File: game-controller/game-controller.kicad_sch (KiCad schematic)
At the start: 0 parts

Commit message: Fixed kicad library manager bug
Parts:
- added U1: STM32F103C8T6, parts:LQFP-48_L7.0-W7.0-P0.50-LS9.0-BL, symbol parts:STM32F103C8T6
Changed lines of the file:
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@@
 	(generator_version "10.0")
 	(paper "A4")
+	(symbol
+		(lib_id "parts:STM32F103C8T6")
+		(at 132.08 93.98 0)
+		(unit 1)
+		(body_style 1)
+		(exclude_from_sim no)
+		(in_bom yes)
+		(on_board yes)
+		(in_pos_files yes)
+		(dnp no)
+		(fields_autoplaced yes)
+		(property "Reference" "U1"
+			(at 132.08 57.15 0)
+			(show_name no)
+			(do_not_autoplace no)
+			(effects
+				(font
+					(size 1.27 1.27)
+				)
+			)
+		)
+		(property "Value" "STM32F103C8T6"
+			(at 132.08 59.69 0)
+			(show_name no)
+			(do_not_autoplace no)
+			(effects
+				(font
+					(size 1.27 1.27)
+				)
+			)
+		)
+		(property "Footprint" "parts:LQFP-48_L7.0-W7.0-P0.50-LS9.0-BL"
+			(at 132.08 130.81 0)
+			(hide yes)
+			(show_name no)
+			(do_not_autoplace no)
+			(effects
+				(font
+					(size 1.27 1.27)
+				)
+			)
+		)
+		(property "Datasheet" "https://lcsc.com/product-detail/ST-Microelectronics_STMicroelectronics_STM32F103C8T6_STM32F103C8T6_C8734.html"
+			(at 132.08 133.35 0)
+			(hide yes)
+			(show_name no)
+			(do_not_autoplace no)
+			(effects
+				(font
+					(size 1.27 1.27)
+				)
+			)
+		)
+		(property "Description" "ARM Cortex-M3 32-bit MCU, 64 KB Flash, 20 KB Internal RAM, 37 IOs, 48-pin LQFP, -40 to 85 degC, Tray"
+			(at 132.08 93.98 0)
+			(hide yes)
+			(show_name no)
+			(do_not_autoplace no)
+			(effects
+				(font
+					(size 1.27 1.27)
+				)
+			)
+		)
+		(property "Manufacturer" "ST(意法半导体)"
+			(at 132.08 135.89 0)
+			(hide yes)
+			(show_name no)
+			(do_not_autoplace no)
+			(effects
+				(font
+					(size 1.27 1.27)
+				)
+			)
+		)
+		(property "MPN" "STM32F103C8T6"
+			(at 132.08 138.43 0)
+			(hide yes)
+			(show_name no)
+			(do_not_autoplace no)
+			(effects
+				(font
+					(size 1.27 1.27)
+				)
+			)
+		)
+		(property "LCSC Part" "C8734"
+			(at 132.08 140.97 0)
+			(hide yes)
+			(show_name no)
+			(do_not_autoplace no)
+			(effects
+				(font
+					(size 1.27 1.27)
+				)
+			)
+		)
+		(pin "15"
+		)
+		(pin "30"
+		)
+		(pin "41"
+		)
+		(pin "28"
+		)
+		(pin "27"
+		)
+		(pin "26"
+		)
+		(pin "17"
+		)
+		(pin "25"
+		)
+		(pin "32"
+		)
+		(pin "24"
+		)
+		(pin "23"
+		)
+		(pin "22"
+		)
+		(pin "21"
+		)
+		(pin "20"
+		)
+		(pin "18"
+		)
+		(pin "19"
+		)
+		(pin "34"
+		)
+		(pin "48"
+		)
+		(pin "47"
+		)
+		(pin "9"
+		)
+		(pin "8"
+		)
+		(pin "7"
+		)
+		(pin "6"
+		)
+		(pin "5"
+		)
+		(pin "4"
+		)
+		(pin "3"
+		)
+		(pin "2"
+		)
+		(pin "1"
+		)
+		(pin "46"
+		)
+		(pin "45"
+		)
+		(pin "29"
+		)
+		(pin "13"
+		)
+		(pin "12"
+		)
+		(pin "11"
+		)
+		(pin "10"
+		)
+		(pin "44"
+		)
+		(pin "33"
+		)
+		(pin "43"
+		)
+		(pin "31"
+		)
+		(pin "42"
+		)
+		(pin "16"
+		)
+		(pin "14"
+		)
+		(pin "40"
+		)
+		(pin "38"
+		)
+		(pin "36"
+		)
+		(pin "37"
+		)
+		(pin "39"
+		)
+		(pin "35"
+		)
+		(instances
+			(project "game-controller"
+				(path "/09f2e687-94b8-4ec9-a79c-a1fb25df92c9"
+					(reference "U1")
+					(unit 1)
+				)
+			)
+		)
+	)
 	(sheet_instances
 		(path "/"

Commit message: Schematics to be continued
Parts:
- added C1, C2, C3: 100nF, symbol Device:C
- added C4: 4.7uF, symbol Device:C
- added C5: 10nF, symbol Device:C
- added C6: 1uF, symbol Device:C
- added FPC1, FPC2: AFC07-S05FCC-00, parts:FPC-SMD_AFC07-S05FCC-00, symbol parts:AFC07-S05FCC-00
- added H1: HX PZ2.54-1X5P WT, parts:HDR-SMD_5P-P2.54-H-M-W12.8-N, symbol parts:HXPZ2.54-1X5PWT
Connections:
- net +3.3V: now reaches U1.1 (VBAT)
- net +3.3V: now also U1.24 (VDD_1), U1.36 (VDD_2), U1.48 (VDD_3), U1.9 (VDDA), C1.1, C2.2, C3.1, C4.1, C5.2, C6.2, H1.5
- net GND: now reaches U1.23 (VSS_1)
- net GND: now also U1.35 (VSS_2), U1.47 (VSS_3), U1.8 (VSSA), C1.2, C2.1, C3.2, C4.2, C5.1, C6.1, FPC1.6, FPC1.7, FPC2.6, FPC2.7, H1.3
- net USB_DM: now reaches U1.32 (PA11)
- net USB_DP: now reaches U1.33 (PA12)
- net SWDIO: now reaches U1.34 (PA13)
- net SWDIO: now also H1.2
- net SWCLK: now reaches U1.37 (PA14)
- net SWCLK: now also H1.4
- net NRST: now reaches U1.7 (NRST)
- net NRST: now also H1.1
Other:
- note added: "https://github.com/dekuNukem/Nintendo_Switch_Reverse_Engineering/issues/69"

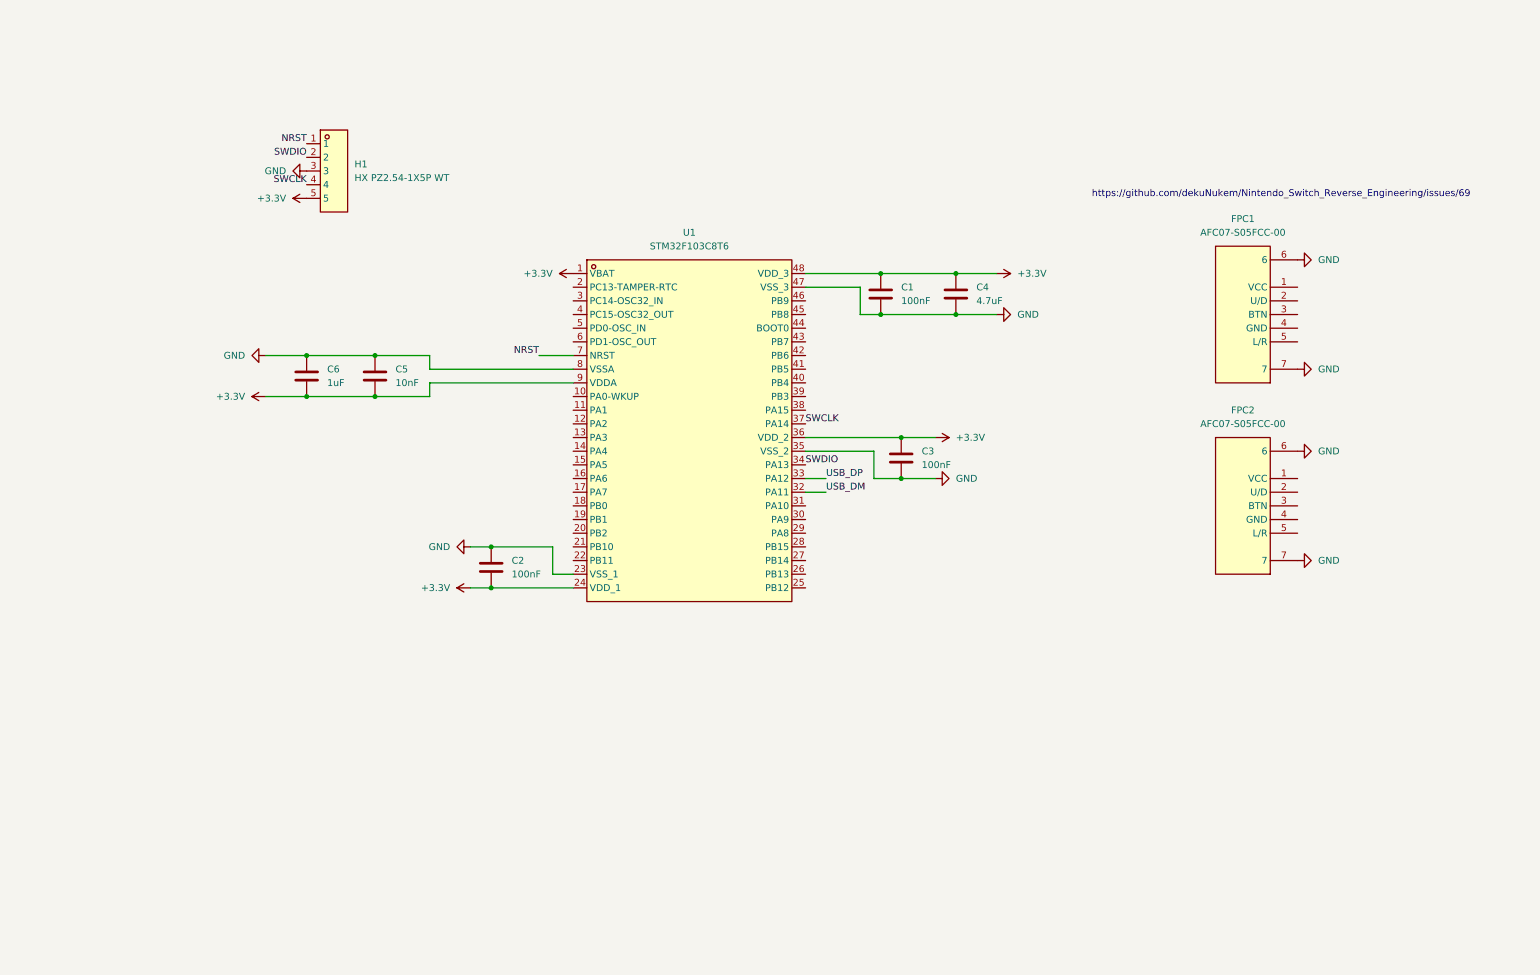
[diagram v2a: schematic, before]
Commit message: Added dpad and buttons to schematics
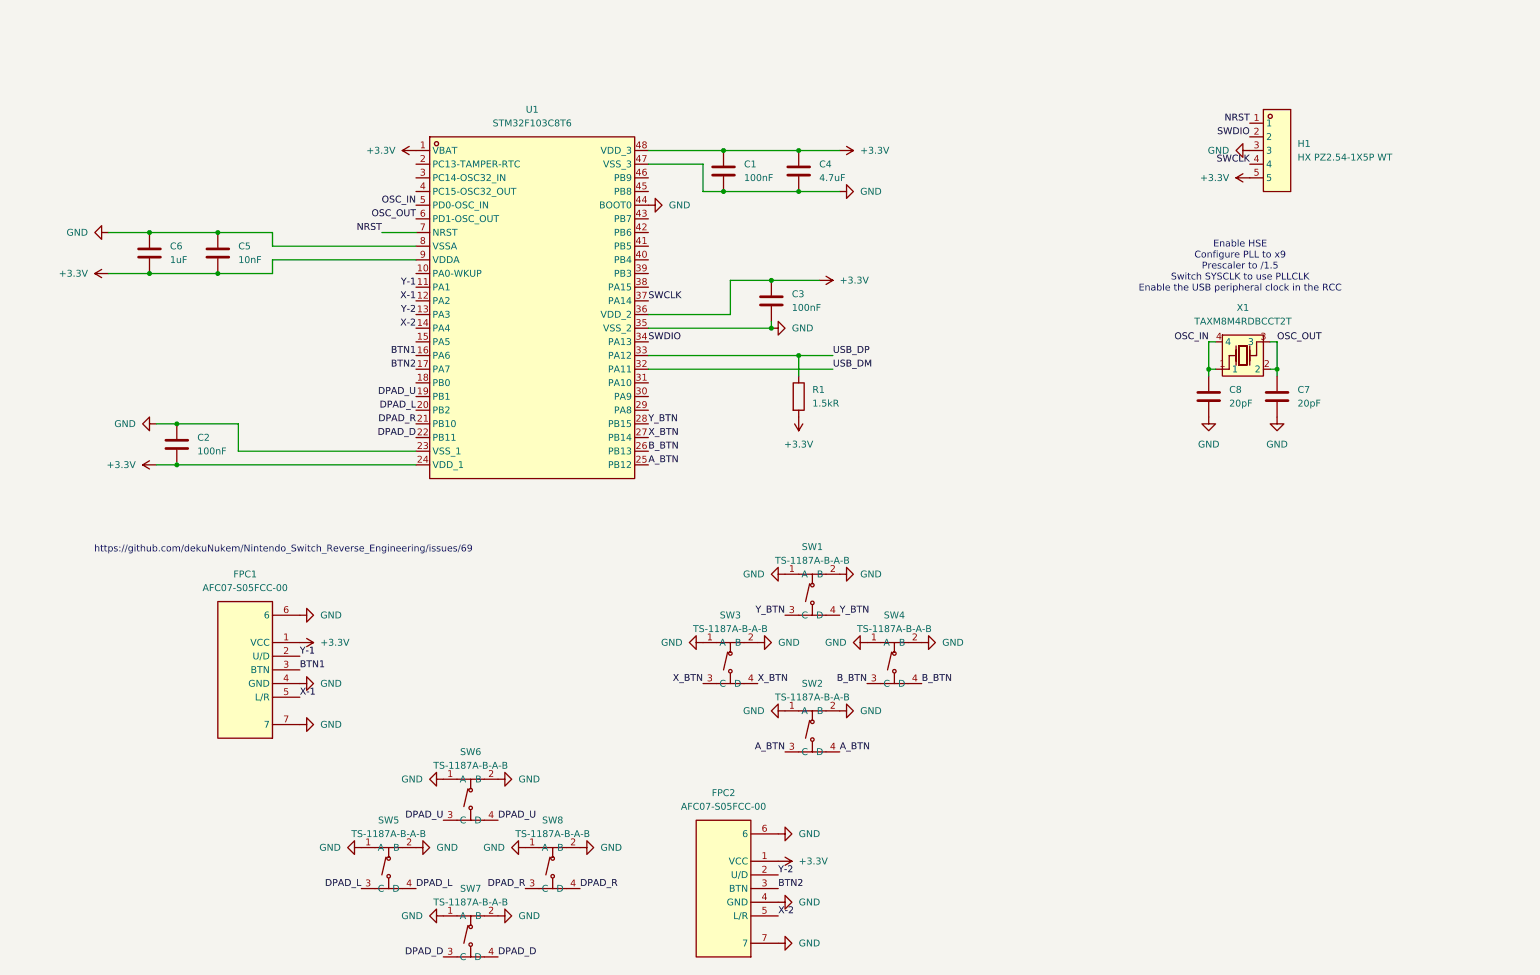
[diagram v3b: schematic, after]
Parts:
- added C7, C8: 20pF, 0402, symbol Device:C
- added R1: 1.5kR, Resistor_SMD:R_0603_1608Metric, symbol Device:R
- added SW1, SW2, SW3, SW4, SW5, SW6, SW7, SW8: TS-1187A-B-A-B, parts:SW-SMD_4P-L5.1-W5.1-P3.70-LS6.5-TL_H1.5, symbol parts:TS-1187A-B-A-B
- added X1: TAXM8M4RDBCCT2T, parts:CRYSTAL-SMD_4P-L3.2-W2.5-BL, symbol parts:TAXM8M4RDBCCT2T
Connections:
- net +3.3V: now also FPC1.1 (VCC), FPC2.1 (VCC), R1.2
- net GND: now also FPC1.4 (GND), FPC2.4 (GND), U1.44 (BOOT0), C7.2, C8.2, SW1.1 (A), SW1.2 (B), SW2.1 (A), SW2.2 (B), SW3.1 (A), SW3.2 (B), SW4.1 (A), SW4.2 (B), SW5.1 (A), SW5.2 (B), SW6.1 (A), SW6.2 (B), SW7.1 (A), SW7.2 (B), SW8.1 (A), SW8.2 (B)
- net USB_DP: now also R1.1
- net Y-2: now reaches FPC2.2 (U/D)
- net Y-2: now also U1.13 (PA3)
- net BTN2: now reaches FPC2.3 (BTN)
- net BTN2: now also U1.17 (PA7)
- net X-2: now reaches FPC2.5 (L/R)
- net X-2: now also U1.14 (PA4)
- net Y-1: now reaches U1.11 (PA1)
- net Y-1: now also FPC1.2 (U/D)
- net X-1: now reaches U1.12 (PA2)
- net X-1: now also FPC1.5 (L/R)
- net BTN1: now reaches U1.16 (PA6)
- net BTN1: now also FPC1.3 (BTN)
- net DPAD_U: now reaches U1.19 (PB1)
- net DPAD_U: now also SW6.3 (C), SW6.4 (D)
- net DPAD_L: now reaches U1.20 (PB2)
- net DPAD_L: now also SW5.3 (C), SW5.4 (D)
- net DPAD_R: now reaches U1.21 (PB10)
- net DPAD_R: now also SW8.3 (C), SW8.4 (D)
- net DPAD_D: now reaches U1.22 (PB11)
- net DPAD_D: now also SW7.3 (C), SW7.4 (D)
- net A_BTN: now reaches U1.25 (PB12)
- net A_BTN: now also SW2.3 (C), SW2.4 (D)
- net B_BTN: now reaches U1.26 (PB13)
- net B_BTN: now also SW4.3 (C), SW4.4 (D)
- net X_BTN: now reaches U1.27 (PB14)
- net X_BTN: now also SW3.3 (C), SW3.4 (D)
- net Y_BTN: now reaches U1.28 (PB15)
- net Y_BTN: now also SW1.3 (C), SW1.4 (D)
- net OSC_IN: now reaches U1.5 (PD0-OSC_IN)
- net OSC_IN: now also C8.1, X1.1, X1.4
- net OSC_OUT: now reaches U1.6 (PD1-OSC_OUT)
- net OSC_OUT: now also C7.1, X1.2, X1.3
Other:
- note added: "Enable HSE Configure PLL to x9 Prescaler to /1.5 Switch SYSCLK to use PLLCLK Enable the USB peripheral clock in the RCC"
- moved on the sheet: C1, C2, C3, C4, C5, C6, FPC1, FPC2, H1, U1

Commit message: Added footprints
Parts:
- removed C1, C2: 100nF, symbol Device:C
- added C10, C9: 100nF/16V, Capacitor_SMD:C_0402_1005Metric, symbol Device:C
- C3: value 100nF -> 100nF/16V; footprint (none) -> Capacitor_SMD:C_0402_1005Metric; LCSC Part (none) -> C328914
- C4: value 4.7uF -> 100nF/16V; footprint (none) -> Capacitor_SMD:C_0402_1005Metric; LCSC Part (none) -> C328914
- C5: value 10nF -> 10nF/50V; footprint (none) -> Capacitor_SMD:C_0402_1005Metric; LCSC Part (none) -> C5137480
- C6: value 1uF -> 1uF/10V; footprint (none) -> Capacitor_SMD:C_0402_1005Metric; LCSC Part (none) -> C22399609
- C7, C8: footprint 0402 -> Capacitor_SMD:C_0402_1005Metric
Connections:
- net +3.3V: now also C10.2, C9.1
- net GND: now also C10.1, C9.2
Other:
- moved on the sheet: C5, C6

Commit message: Schematics pretty solid now, need to check it again later
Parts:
- removed X1: TAXM8M4RDBCCT2T, parts:CRYSTAL-SMD_4P-L3.2-W2.5-BL, symbol parts:TAXM8M4RDBCCT2T
- added C11, C12, C13, C14: 1uF/10V, Capacitor_SMD:C_0402_1005Metric, symbol Device:C
- added C15: 100nF/16V, Capacitor_SMD:C_0402_1005Metric, symbol Device:C
- added D4, D5: PESD5V0H1BSFYL, Diode_SMD:Nexperia_DSN0603-2_0.6x0.3mm_P0.4mm, symbol Device:D_TVS
- added D6: H5VL10B, Diode_SMD:D_SOD-882, symbol Device:D_TVS
- added R2: 10kR/±1%, Resistor_SMD:R_0402_1005Metric, symbol Device:R
- added TP1: TestPoint, TestPoint:TestPoint_Pad_1.5x1.5mm, symbol Connector:TestPoint
- added U2, U4: AP2112K-3.3TRG1, parts:SOT-25-5_L2.9-W1.6-P0.95-LS2.8-BL, symbol parts:AP2112K-3.3TRG1
- added U3: YZ103915020T-04025-02, parts:CONN-SMD_YZ103915020T-04025-01, symbol parts:YZ103915020T-04025-02
- added X1: TAXM8M4RLBDDT2T, parts:CRYSTAL-SMD_4P-L3.2-W2.5-BL, symbol parts:TAXM8M4RLBDDT2T
- C4: value 100nF/16V -> 4.7uF/6.3V; LCSC Part C328914 -> C380302
- R1: value 1.5kR -> 1.5kR/±1%
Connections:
- net +3.3V: now also C12.1, U2.5 (VOUT); no longer C5.2, C6.2, FPC1.1 (VCC), FPC2.1 (VCC), U1.9 (VDDA)
- net GND: now also C11.2, C12.2, C13.2, C14.2, C15.1, D4.1 (A1), D5.1 (A1), D6.1 (A1), R2.1, U2.2 (GND), U2.4 (NC), U3.4, U4.2 (GND), U4.4 (NC); no longer U1.44 (BOOT0)
- net NRST: now also C15.2
- net OSC_IN: now also X1.1, X1.4 (GND)
- net OSC_OUT: now also X1.2 (GND), X1.3
- net USB_DM: now also D5.2 (A2), U3.2
- net USB_DP: now also D4.2 (A2), U3.3
- new net: R2.2, TP1.1, U1.44 (BOOT0)
- new net +3.3VA: C14.1, C5.2, C6.2, FPC1.1 (VCC), FPC2.1 (VCC), U1.9 (VDDA), U4.5 (VOUT)
- new net +5V: C11.1, C13.1, D6.2 (A2), U2.1 (VIN), U2.3 (EN), U3.1, U4.1 (VIN), U4.3 (EN)
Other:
- note added: "4-pin Pogo USB connection"
- note added: "Digital and Analog sources"
- note added: "STLINK"
- moved on the sheet: C10, C3, C4, C5, C6, C7, C8, C9, FPC1, FPC2, H1, R1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

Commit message: Will need to design the connector ourself
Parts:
- removed U3: YZ103915020T-04025-02, parts:CONN-SMD_YZ103915020T-04025-01, symbol parts:YZ103915020T-04025-02
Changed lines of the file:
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@@
-	)
-	(symbol
-		(lib_id "parts:YZ103915020T-04025-02")
-		(at 250.19 78.74 0)
-		(unit 1)
-		(body_style 1)
-		(exclude_from_sim no)
-		(in_bom yes)
-		(on_board yes)
-		(in_pos_files yes)
-		(dnp no)
-		(fields_autoplaced yes)
-		(property "Reference" "U3"
-			(at 255.27 77.4699 0)
-			(show_name no)
-			(do_not_autoplace no)
-			(effects
-				(font
-					(size 1.27 1.27)
-				)
-				(justify left)
-			)
-		)
-		(property "Value" "YZ103915020T-04025-02"
-			(at 255.27 80.0099 0)
-			(show_name no)
-			(do_not_autoplace no)
-			(effects
-				(font
-					(size 1.27 1.27)
-				)
-				(justify left)
-			)
-		)
-		(property "Footprint" "parts:CONN-SMD_YZ103915020T-04025-01"
-			(at 250.19 90.17 0)
-			(hide yes)
-			(show_name no)
-			(do_not_autoplace no)
-			(effects
-				(font
-					(size 1.27 1.27)
-				)
-			)
-		)
-		(property "Datasheet" "https://www.lcsc.com/datasheet/C6276862.pdf"
-			(at 250.19 92.71 0)
-			(hide yes)
-			(show_name no)
-			(do_not_autoplace no)
-			(effects
-				(font
-					(size 1.27 1.27)
-				)
-			)
-		)
-		(property "Description" ""
-			(at 250.19 78.74 0)
-			(hide yes)
-			(show_name no)
-			(do_not_autoplace no)
-			(effects
-				(font
-					(size 1.27 1.27)
-				)
-			)
-		)
-		(property "Manufacturer" "Xinyangze(鑫扬泽)"
-			(at 250.19 95.25 0)
-			(hide yes)
-			(show_name no)
-			(do_not_autoplace no)
-			(effects
-				(font
-					(size 1.27 1.27)
-				)
-			)
-		)
-		(property "MPN" "YZ103915020T-04025-02"
-			(at 250.19 97.79 0)
-			(hide yes)
-			(show_name no)
-			(do_not_autoplace no)
-			(effects
-				(font
-					(size 1.27 1.27)
-				)
-			)
-		)
-		(property "LCSC Part" "C6276862"
-			(at 250.19 100.33 0)
-			(hide yes)
-			(show_name no)
-			(do_not_autoplace no)
-			(effects
-				(font
-					(size 1.27 1.27)
-				)
-			)
-		)
-		(pin "3"
-		)
-		(pin "2"
-		)
-		(pin "4"
-		)
-		(pin "1"
-		)
-		(instances
-			(project "game-controller"
-				(path "/09f2e687-94b8-4ec9-a79c-a1fb25df92c9"
-					(reference "U3")
-					(unit 1)
-				)
-			)
-		)
 	)
 	(symbol
